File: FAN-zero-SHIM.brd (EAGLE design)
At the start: 30 x 65 mm, 6 parts

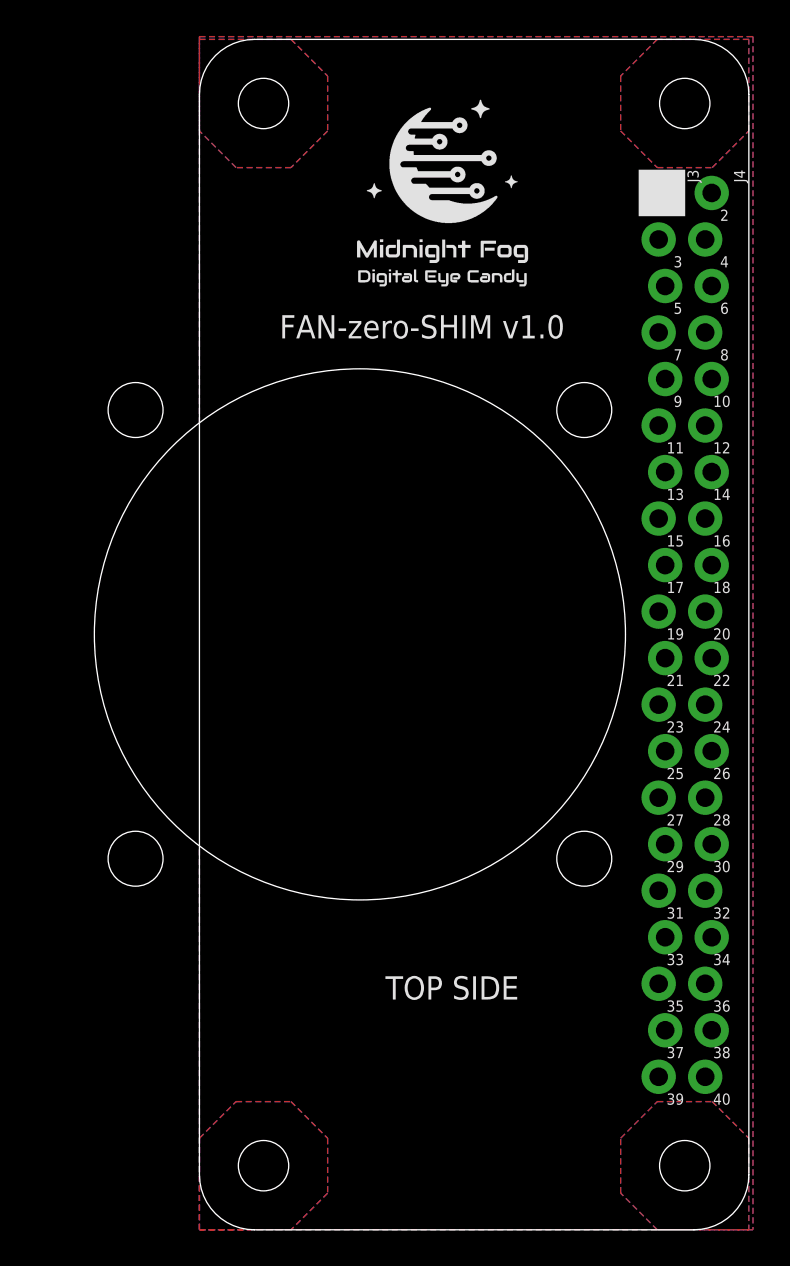
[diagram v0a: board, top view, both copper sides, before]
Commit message: Added basic placement for zero board
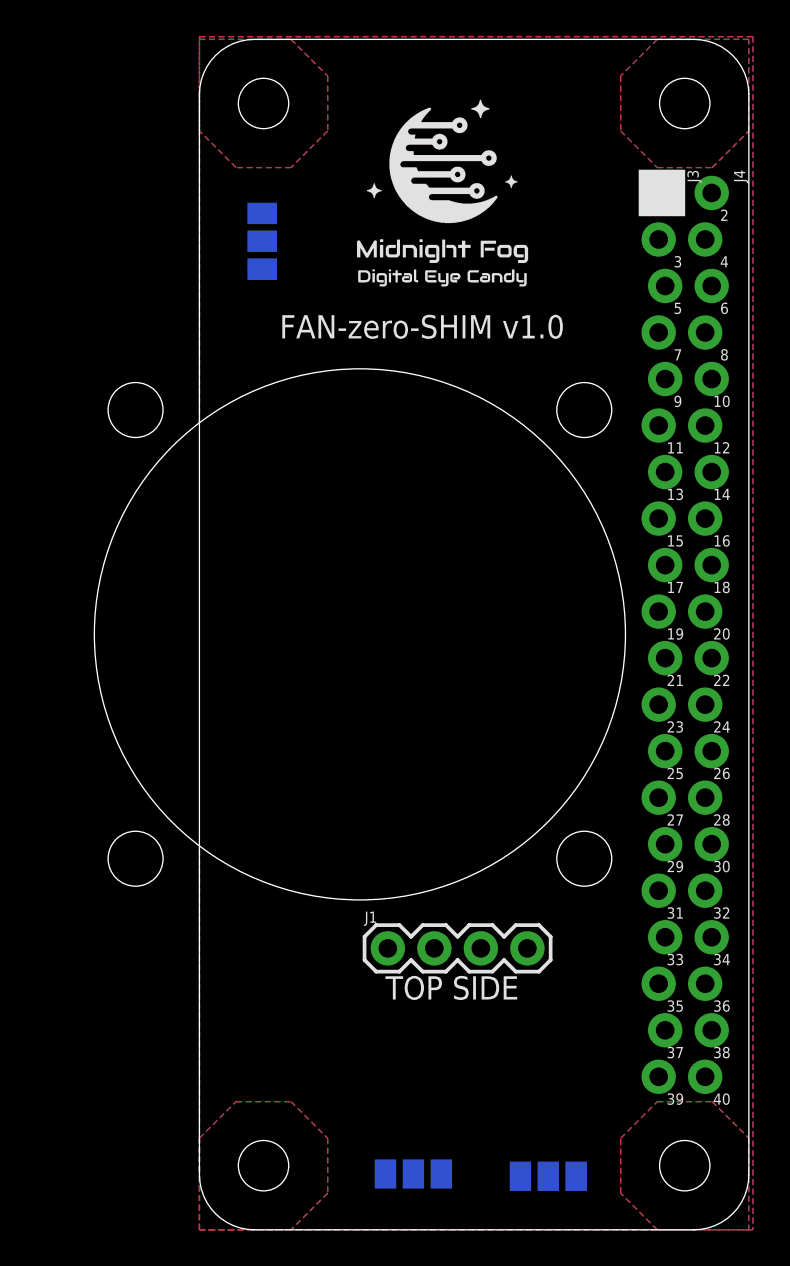
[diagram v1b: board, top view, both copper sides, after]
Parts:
- added J1: (no value), SparkFun-Connectors:1X04
- added SJ1, SJ2, SJ3: (no value), _my_jumpers:SJ_2
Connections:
- new net PWM: J1.4, SJ3.2
- new net TACH: J1.3, SJ2.2
- new net VFAN: J1.2, SJ1.2
- net 3.3V: now also SJ1.3
- net 5V: now also SJ1.1
- net GND: now also J1.1
- net GPIO12: now also SJ3.1
- net GPIO13: now also SJ3.3
- net GPIO16: now also SJ2.1
- net GPIO4: now also SJ2.3
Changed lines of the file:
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@@
 <elements>
 <element name="J3" library="_my_locked_connectors" package="1X20_LOCK" value="" x="25.254" y="56.615" smashed="yes" rot="R270">
-<attribute name="NAME" x="26.651" y="57.885" size="0.6096" layer="25" font="vector" ratio="20" rot="R270"/>
+<attribute name="NAME" x="26.651" y="57.885" size="0.6096" layer="25" font="vector" rot="R270"/>
 <attribute name="VALUE" x="23.222" y="57.885" size="0.6096" layer="27" font="vector" ratio="20" rot="R270"/>
 </element>
 <element name="J4" library="_my_locked_connectors" package="1X20_LOCK" value="" x="27.794" y="56.615" smashed="yes" rot="R270">
-<attribute name="NAME" x="29.191" y="57.885" size="0.6096" layer="25" font="vector" ratio="20" rot="R270"/>
+<attribute name="NAME" x="29.191" y="57.885" size="0.6096" layer="25" font="vector" rot="R270"/>
 <attribute name="VALUE" x="25.762" y="57.885" size="0.6096" layer="27" font="vector" ratio="20" rot="R270"/>
 </element>
@@
 <element name="LOGO2" library="_my_logos" package="MFDEC_SQ_8MM" value="MFDECLOGO_SQ_8MM" x="7.927" y="51.212" smashed="yes"/>
 <element name="LOGO3" library="_my_logos" package="RSNURL_QR_10MM" value="RSNURL_QR_10MM" x="18.087" y="51.212" smashed="yes" rot="MR0"/>
+<element name="J1" library="SparkFun-Connectors" library_urn="urn:adsk.eagle:library:513" package="1X04" package3d_urn="urn:adsk.eagle:package:38085/1" value="" x="10.287" y="15.367" smashed="yes">
+<attribute name="NAME" x="9.017" y="16.764" size="0.6096" layer="25" font="vector"/>
+<attribute name="PROD_ID" value="CONN-09696" x="10.287" y="27.94" size="1.778" layer="27" display="off"/>
+<attribute name="VALUE" x="9.017" y="13.335" size="0.6096" layer="27" font="vector" ratio="20"/>
+</element>
+<element name="SJ1" library="_my_jumpers" package="SJ_2" value="" x="3.429" y="53.975" smashed="yes" rot="MR90">
+<attribute name="NAME" x="4.699" y="51.562" size="0.6096" layer="26" font="vector" rot="MR90"/>
+<attribute name="VALUE" x="3.429" y="53.8749" size="0.02" layer="28" rot="MR90"/>
+</element>
+<element name="SJ2" library="_my_jumpers" package="SJ_2" value="" x="19.05" y="2.921" smashed="yes" rot="MR0">
+<attribute name="NAME" x="21.463" y="4.191" size="0.6096" layer="26" font="vector" rot="MR0"/>
+<attribute name="VALUE" x="19.1501" y="2.921" size="0.02" layer="28" rot="MR0"/>
+</element>
+<element name="SJ3" library="_my_jumpers" package="SJ_2" value="" x="11.684" y="3.048" smashed="yes" rot="MR0">
+<attribute name="NAME" x="14.097" y="4.318" size="0.6096" layer="26" font="vector" rot="MR0"/>
+<attribute name="VALUE" x="11.7841" y="3.048" size="0.02" layer="28" rot="MR0"/>
+</element>
 </elements>
 <signals>
@@
 <vertex x="30.226" y="0"/>
 </polygon>
+<contactref element="J1" pad="1"/>
 <wire x1="25.4318" y1="46.455" x2="27.9718" y2="51.535" width="0" layer="19" extent="1-1"/>
 <wire x1="27.9718" y1="41.375" x2="25.4318" y2="46.455" width="0" layer="19" extent="1-1"/>
@@
 <wire x1="27.9718" y1="15.975" x2="27.9718" y2="21.055" width="0" layer="19" extent="1-1"/>
 <wire x1="25.0762" y1="8.355" x2="27.9718" y2="15.975" width="0" layer="19" extent="1-1"/>
+<wire x1="10.287" y1="15.367" x2="25.0762" y2="8.355" width="0" layer="19" extent="1-1"/>
 </signal>
 <signal name="3.3V">
 <contactref element="J3" pad="1"/>
 <contactref element="J3" pad="9"/>
+<contactref element="SJ1" pad="3"/>
 <wire x1="25.4318" y1="36.295" x2="25.4318" y2="56.615" width="0" layer="19" extent="1-1"/>
+<wire x1="3.429" y1="55.499" x2="25.4318" y2="36.295" width="0" layer="19" extent="1-1"/>
 </signal>
 <signal name="GPIO2">
@@
 <signal name="GPIO4">
 <contactref element="J3" pad="4"/>
+<contactref element="SJ2" pad="3"/>
+<wire x1="17.526" y1="2.921" x2="25.0762" y2="48.995" width="0" layer="19" extent="1-1"/>
 </signal>
 <signal name="GPIO17">
@@
 <signal name="GPIO13">
 <contactref element="J3" pad="17"/>
+<contactref element="SJ3" pad="3"/>
+<wire x1="10.16" y1="3.048" x2="25.4318" y2="15.975" width="0" layer="19" extent="1-1"/>
 </signal>
 <signal name="GPIO19">
@@
 <signal name="GPIO12">
 <contactref element="J4" pad="16"/>
+<contactref element="SJ3" pad="1"/>
+<wire x1="13.208" y1="3.048" x2="27.6162" y2="18.515" width="0" layer="19" extent="1-1"/>
 </signal>
 <signal name="GPIO16">
 <contactref element="J4" pad="18"/>
+<contactref element="SJ2" pad="1"/>
+<wire x1="20.574" y1="2.921" x2="27.6162" y2="13.435" width="0" layer="19" extent="1-1"/>
 </signal>
 <signal name="GPIO20">
@@
 <contactref element="J4" pad="1"/>
 <contactref element="J4" pad="2"/>
+<contactref element="SJ1" pad="1"/>
 <wire x1="27.6162" y1="54.075" x2="27.9718" y2="56.615" width="0" layer="19" extent="1-1"/>
+<wire x1="3.429" y1="52.451" x2="27.6162" y2="54.075" width="0" layer="19" extent="1-1"/>
 </signal>
 <signal name="GND1" airwireshidden="yes">
@@
 <vertex x="30" y="60"/>
 </polygon>
+</signal>
+<signal name="VFAN">
+<contactref element="J1" pad="2"/>
+<contactref element="SJ1" pad="2"/>
+<wire x1="3.429" y1="53.975" x2="12.827" y2="15.367" width="0" layer="19" extent="1-1"/>
+</signal>
+<signal name="TACH">
+<contactref element="J1" pad="3"/>
+<contactref element="SJ2" pad="2"/>
+<wire x1="19.05" y1="2.921" x2="15.367" y2="15.367" width="0" layer="19" extent="1-1"/>
+</signal>
+<signal name="PWM">
+<contactref element="J1" pad="4"/>
+<contactref element="SJ3" pad="2"/>
+<wire x1="11.684" y1="3.048" x2="17.907" y2="15.367" width="0" layer="19" extent="1-1"/>
 </signal>
 </signals>
@@
 </board>
 </drawing>
+<compatibility>
+<note version="8.2" severity="warning">
+Since Version 8.2, EAGLE supports online libraries. The ids
+of those online libraries will not be understood (or retained)
+with this version.
+</note>
+<note version="8.3" severity="warning">
+Since Version 8.3, EAGLE supports URNs for individual library
+assets (packages, symbols, and devices). The URNs of those assets
+will not be understood (or retained) with this version.
+</note>
+<note version="8.3" severity="warning">
+Since Version 8.3, EAGLE supports the association of 3D packages
+with devices in libraries, schematics, and board files. Those 3D
+packages will not be understood (or retained) with this version.
+</note>
+</compatibility>
 </eagle>

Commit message: Shaped FAN-zero-SHIM size.
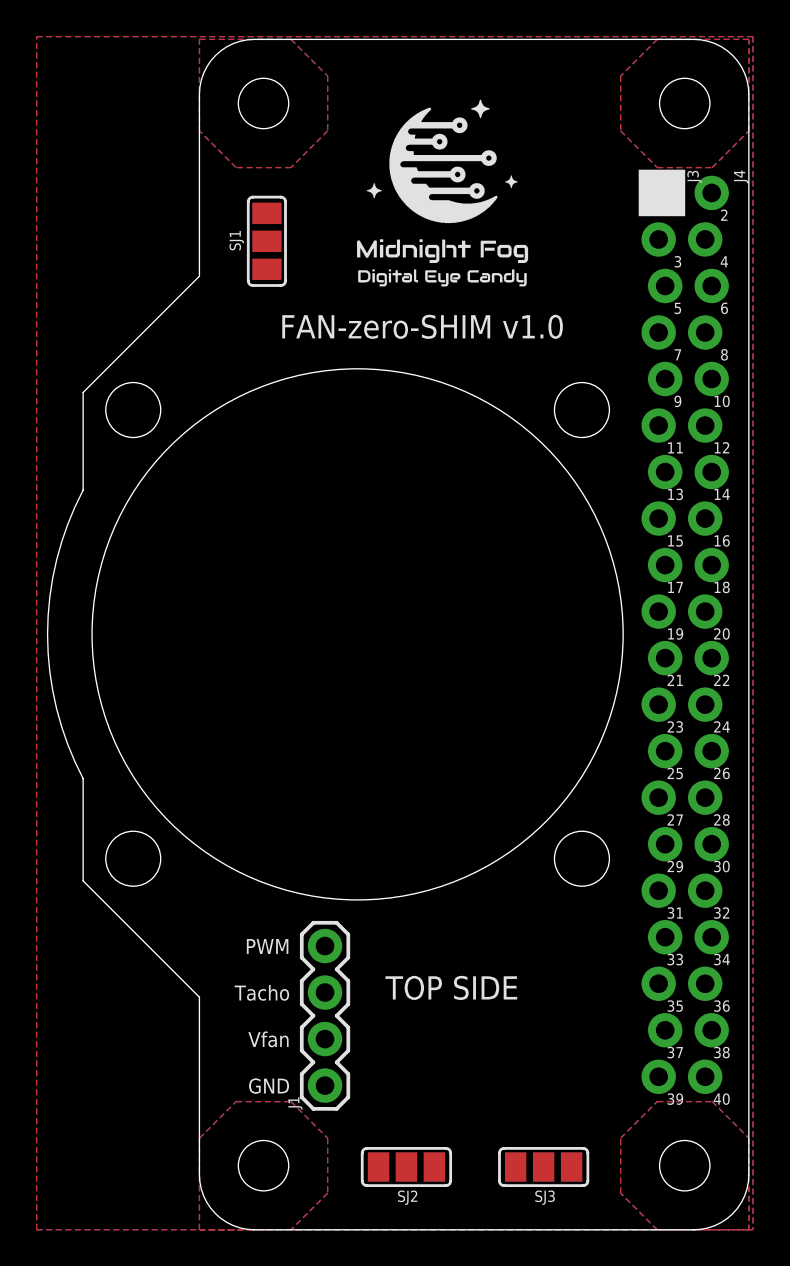
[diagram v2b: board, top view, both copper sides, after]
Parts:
- moved J1 8.24 mm to (6.86, 7.87), turned to 90 degrees
- moved SJ2 7.76 mm to (11.3, 3.43), flipped to the top, turned to 180 degrees
- moved SJ3 7.12 mm to (18.8, 3.43), flipped to the top, turned to 180 degrees
- moved SJ1 0.25 mm to (3.68, 54.0), flipped to the top
- moved FAN1 0.13 mm to (8.64, 32.5)
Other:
- board size 30 x 65 mm -> 38.3 x 65 mm
- board text added: "GND"
- board text added: "PWM"
- board text added: "Tacho"
- board text added: "Vfan"
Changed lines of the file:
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@@
 <wire x1="30" y1="3" x2="30" y2="62" width="0" layer="20"/>
 <wire x1="27" y1="65" x2="3" y2="65" width="0" layer="20"/>
-<wire x1="0" y1="62" x2="0" y2="3" width="0" layer="20"/>
-<wire x1="3" y1="0" x2="0" y2="3" width="0" layer="20" curve="-90"/>
-<wire x1="0" y1="62" x2="3" y2="65" width="0" layer="20" curve="-90"/>
+<wire x1="3" y1="0" x2="0" y2="2.9972" width="0" layer="20" curve="-89.946524"/>
+<wire x1="0" y1="2.9972" x2="0" y2="3" width="0" layer="20" curve="-0.053476"/>
+<wire x1="0" y1="62" x2="0" y2="62.0014" width="0" layer="20" curve="-0.026738"/>
+<wire x1="0" y1="62.0014" x2="3" y2="65" width="0" layer="20" curve="-89.973262"/>
 <wire x1="27" y1="65" x2="30" y2="62" width="0" layer="20" curve="-90"/>
 <wire x1="30" y1="3" x2="27" y2="0" width="0" layer="20" curve="-90"/>
@@
 <text x="19.357" y="49.307" size="1.016" layer="22" font="vector" ratio="12" rot="MR0">http://redscorp.net</text>
 <text x="19.357" y="48.037" size="1.016" layer="22" font="vector" ratio="12" rot="MR0">(c) Andriy Golovnya</text>
+<wire x1="0" y1="2.9972" x2="0" y2="12.7" width="0" layer="20"/>
+<wire x1="0" y1="12.7" x2="-6.35" y2="19.05" width="0" layer="20"/>
+<wire x1="0" y1="62.0014" x2="0" y2="52.07" width="0" layer="20"/>
+<wire x1="0" y1="52.07" x2="-6.35" y2="45.72" width="0" layer="20"/>
+<wire x1="-6.35" y1="24.638" x2="-6.35" y2="40.386" width="0" layer="20" curve="-55.437"/>
+<wire x1="-6.35" y1="19.05" x2="-6.35" y2="24.638" width="0" layer="20"/>
+<wire x1="-6.35" y1="45.72" x2="-6.35" y2="40.386" width="0" layer="20"/>
+<text x="4.953" y="8.255" size="0.8128" layer="21" font="vector" rot="R180">GND</text>
+<text x="4.953" y="10.795" size="0.8128" layer="21" font="vector" rot="R180">Vfan</text>
+<text x="4.953" y="13.335" size="0.8128" layer="21" font="vector" rot="R180">Tacho</text>
+<text x="4.953" y="15.875" size="0.8128" layer="21" font="vector" rot="R180">PWM</text>
 </plain>
 <attributes>
@@
 </element>
 <element name="LOGO1" library="_my_logos" package="MFDEC_L_30MM" value="MFDECLOGO_L_30MM" x="-4.191" y="-7.112" smashed="yes" rot="MR90"/>
-<element name="FAN1" library="_my_fans" package="FAN30HO" value="FAN30HO" x="8.763" y="32.512" smashed="yes"/>
+<element name="FAN1" library="_my_fans" package="FAN30HO" value="FAN30HO" x="8.636" y="32.512" smashed="yes"/>
 <element name="LOGO2" library="_my_logos" package="MFDEC_SQ_8MM" value="MFDECLOGO_SQ_8MM" x="7.927" y="51.212" smashed="yes"/>
 <element name="LOGO3" library="_my_logos" package="RSNURL_QR_10MM" value="RSNURL_QR_10MM" x="18.087" y="51.212" smashed="yes" rot="MR0"/>
-<element name="J1" library="SparkFun-Connectors" library_urn="urn:adsk.eagle:library:513" package="1X04" package3d_urn="urn:adsk.eagle:package:38085/1" value="" x="10.287" y="15.367" smashed="yes">
-<attribute name="NAME" x="9.017" y="16.764" size="0.6096" layer="25" font="vector"/>
-<attribute name="PROD_ID" value="CONN-09696" x="10.287" y="27.94" size="1.778" layer="27" display="off"/>
-<attribute name="VALUE" x="9.017" y="13.335" size="0.6096" layer="27" font="vector" ratio="20"/>
-</element>
-<element name="SJ1" library="_my_jumpers" package="SJ_2" value="" x="3.429" y="53.975" smashed="yes" rot="MR90">
-<attribute name="NAME" x="4.699" y="51.562" size="0.6096" layer="26" font="vector" rot="MR90"/>
-<attribute name="VALUE" x="3.429" y="53.8749" size="0.02" layer="28" rot="MR90"/>
-</element>
-<element name="SJ2" library="_my_jumpers" package="SJ_2" value="" x="19.05" y="2.921" smashed="yes" rot="MR0">
-<attribute name="NAME" x="21.463" y="4.191" size="0.6096" layer="26" font="vector" rot="MR0"/>
-<attribute name="VALUE" x="19.1501" y="2.921" size="0.02" layer="28" rot="MR0"/>
-</element>
-<element name="SJ3" library="_my_jumpers" package="SJ_2" value="" x="11.684" y="3.048" smashed="yes" rot="MR0">
-<attribute name="NAME" x="14.097" y="4.318" size="0.6096" layer="26" font="vector" rot="MR0"/>
-<attribute name="VALUE" x="11.7841" y="3.048" size="0.02" layer="28" rot="MR0"/>
+<element name="J1" library="SparkFun-Connectors" library_urn="urn:adsk.eagle:library:513" package="1X04" package3d_urn="urn:adsk.eagle:package:38085/1" value="" x="6.858" y="7.874" smashed="yes" rot="R90">
+<attribute name="NAME" x="5.461" y="6.604" size="0.6096" layer="25" font="vector" rot="R90"/>
+<attribute name="PROD_ID" value="CONN-09696" x="-5.715" y="7.874" size="1.778" layer="27" rot="R90" display="off"/>
+<attribute name="VALUE" x="8.89" y="6.604" size="0.6096" layer="27" font="vector" ratio="20" rot="R90"/>
+</element>
+<element name="SJ1" library="_my_jumpers" package="SJ_2" value="" x="3.683" y="53.975" smashed="yes" rot="R90">
+<attribute name="NAME" x="1.651" y="54.61" size="0.6096" layer="25" font="vector" rot="R270"/>
+<attribute name="VALUE" x="3.683" y="53.8749" size="0.02" layer="27" rot="R90"/>
+</element>
+<element name="SJ2" library="_my_jumpers" package="SJ_2" value="" x="11.303" y="3.429" smashed="yes" rot="R180">
+<attribute name="NAME" x="10.795" y="1.524" size="0.6096" layer="25" font="vector"/>
+<attribute name="VALUE" x="11.4031" y="3.429" size="0.02" layer="27" rot="R180"/>
+</element>
+<element name="SJ3" library="_my_jumpers" package="SJ_2" value="" x="18.796" y="3.429" smashed="yes" rot="R180">
+<attribute name="NAME" x="18.288" y="1.524" size="0.6096" layer="25" font="vector"/>
+<attribute name="VALUE" x="18.8961" y="3.429" size="0.02" layer="27" rot="R180"/>
 </element>
 </elements>
@@
 <contactref element="J4" pad="17"/>
 <polygon width="0.1524" layer="1" isolate="0.254" thermals="no">
-<vertex x="0" y="0"/>
-<vertex x="0" y="65.151"/>
+<vertex x="-8.89" y="0"/>
+<vertex x="-8.89" y="65.151"/>
 <vertex x="30.226" y="65.151"/>
 <vertex x="30.226" y="0"/>
 </polygon>
 <polygon width="0.1524" layer="16" isolate="0.254" thermals="no">
-<vertex x="0" y="0"/>
-<vertex x="0" y="65.151"/>
+<vertex x="-8.89" y="0"/>
+<vertex x="-8.89" y="65.151"/>
 <vertex x="30.226" y="65.151"/>
 <vertex x="30.226" y="0"/>
@@
 <wire x1="27.9718" y1="15.975" x2="27.9718" y2="21.055" width="0" layer="19" extent="1-1"/>
 <wire x1="25.0762" y1="8.355" x2="27.9718" y2="15.975" width="0" layer="19" extent="1-1"/>
-<wire x1="10.287" y1="15.367" x2="25.0762" y2="8.355" width="0" layer="19" extent="1-1"/>
+<wire x1="6.858" y1="7.874" x2="25.0762" y2="8.355" width="0" layer="19" extent="1-1"/>
 </signal>
 <signal name="3.3V">
@@
 <contactref element="SJ1" pad="3"/>
 <wire x1="25.4318" y1="36.295" x2="25.4318" y2="56.615" width="0" layer="19" extent="1-1"/>
-<wire x1="3.429" y1="55.499" x2="25.4318" y2="36.295" width="0" layer="19" extent="1-1"/>
+<wire x1="3.683" y1="55.499" x2="25.4318" y2="56.615" width="0" layer="19" extent="16-16"/>
 </signal>
 <signal name="GPIO2">
@@
 <contactref element="J3" pad="4"/>
 <contactref element="SJ2" pad="3"/>
-<wire x1="17.526" y1="2.921" x2="25.0762" y2="48.995" width="0" layer="19" extent="1-1"/>
+<wire x1="9.779" y1="3.429" x2="25.0762" y2="48.995" width="0" layer="19" extent="1-1"/>
 </signal>
 <signal name="GPIO17">
@@
 <contactref element="J3" pad="17"/>
 <contactref element="SJ3" pad="3"/>
-<wire x1="10.16" y1="3.048" x2="25.4318" y2="15.975" width="0" layer="19" extent="1-1"/>
+<wire x1="17.272" y1="3.429" x2="25.4318" y2="15.975" width="0" layer="19" extent="1-1"/>
 </signal>
 <signal name="GPIO19">
@@
 <contactref element="J4" pad="16"/>
 <contactref element="SJ3" pad="1"/>
-<wire x1="13.208" y1="3.048" x2="27.6162" y2="18.515" width="0" layer="19" extent="1-1"/>
+<wire x1="20.32" y1="3.429" x2="27.6162" y2="18.515" width="0" layer="19" extent="1-1"/>
 </signal>
 <signal name="GPIO16">
 <contactref element="J4" pad="18"/>
 <contactref element="SJ2" pad="1"/>
-<wire x1="20.574" y1="2.921" x2="27.6162" y2="13.435" width="0" layer="19" extent="1-1"/>
+<wire x1="12.827" y1="3.429" x2="27.6162" y2="13.435" width="0" layer="19" extent="1-1"/>
 </signal>
 <signal name="GPIO20">
@@
 <contactref element="SJ1" pad="1"/>
 <wire x1="27.6162" y1="54.075" x2="27.9718" y2="56.615" width="0" layer="19" extent="1-1"/>
-<wire x1="3.429" y1="52.451" x2="27.6162" y2="54.075" width="0" layer="19" extent="1-1"/>
+<wire x1="3.683" y1="52.451" x2="27.6162" y2="54.075" width="0" layer="19" extent="16-16"/>
 </signal>
 <signal name="GND1" airwireshidden="yes">
@@
 <contactref element="J1" pad="2"/>
 <contactref element="SJ1" pad="2"/>
-<wire x1="3.429" y1="53.975" x2="12.827" y2="15.367" width="0" layer="19" extent="1-1"/>
+<wire x1="6.858" y1="10.414" x2="3.683" y2="53.975" width="0" layer="19" extent="16-16"/>
 </signal>
 <signal name="TACH">
 <contactref element="J1" pad="3"/>
 <contactref element="SJ2" pad="2"/>
-<wire x1="19.05" y1="2.921" x2="15.367" y2="15.367" width="0" layer="19" extent="1-1"/>
+<wire x1="11.303" y1="3.429" x2="6.858" y2="12.954" width="0" layer="19" extent="1-1"/>
 </signal>
 <signal name="PWM">
 <contactref element="J1" pad="4"/>
 <contactref element="SJ3" pad="2"/>
-<wire x1="11.684" y1="3.048" x2="17.907" y2="15.367" width="0" layer="19" extent="1-1"/>
+<wire x1="18.796" y1="3.429" x2="6.858" y2="15.494" width="0" layer="19" extent="1-1"/>
 </signal>
 </signals>
